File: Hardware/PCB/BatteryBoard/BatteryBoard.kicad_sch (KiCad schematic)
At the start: 79 parts, among them J1 USB_C_Receptacle_USB2.0, J2 Thermistor, J3 Conn_01x07, J4 Conn_01x07, J5 Conn_01x07, J6 Conn_01x07, J7 Power, Q1 FDS4935A, Q2 FDS4935A, SW1 SW_SPDT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

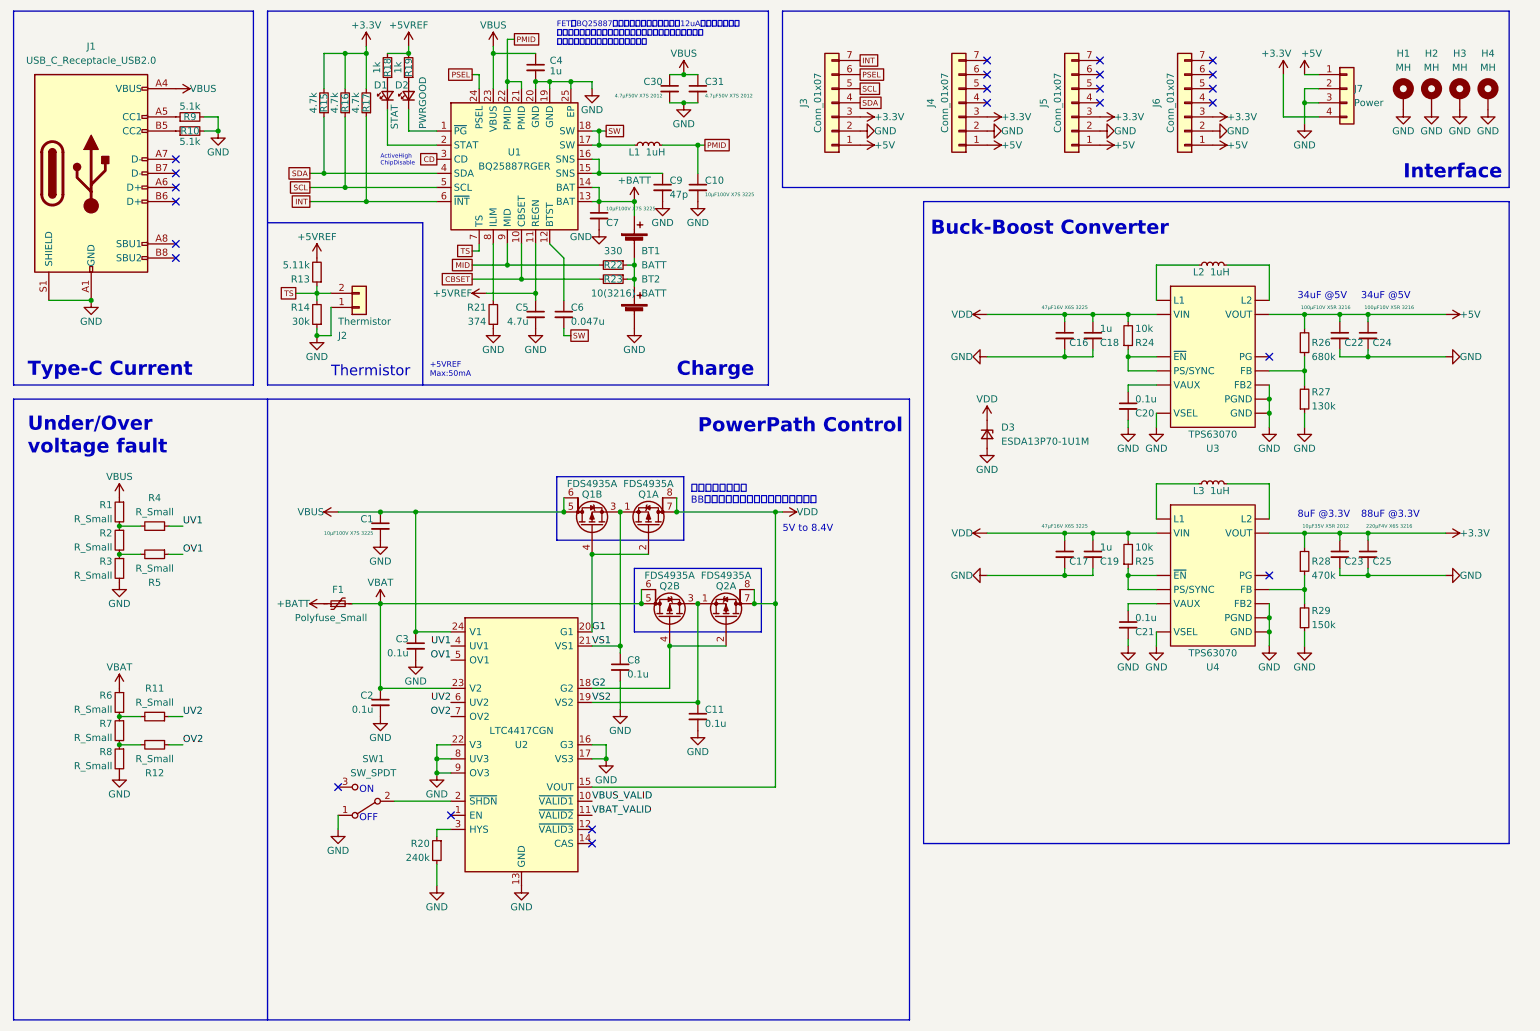
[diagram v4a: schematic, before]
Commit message: 電源ボード製作完了、抵抗の値を反映
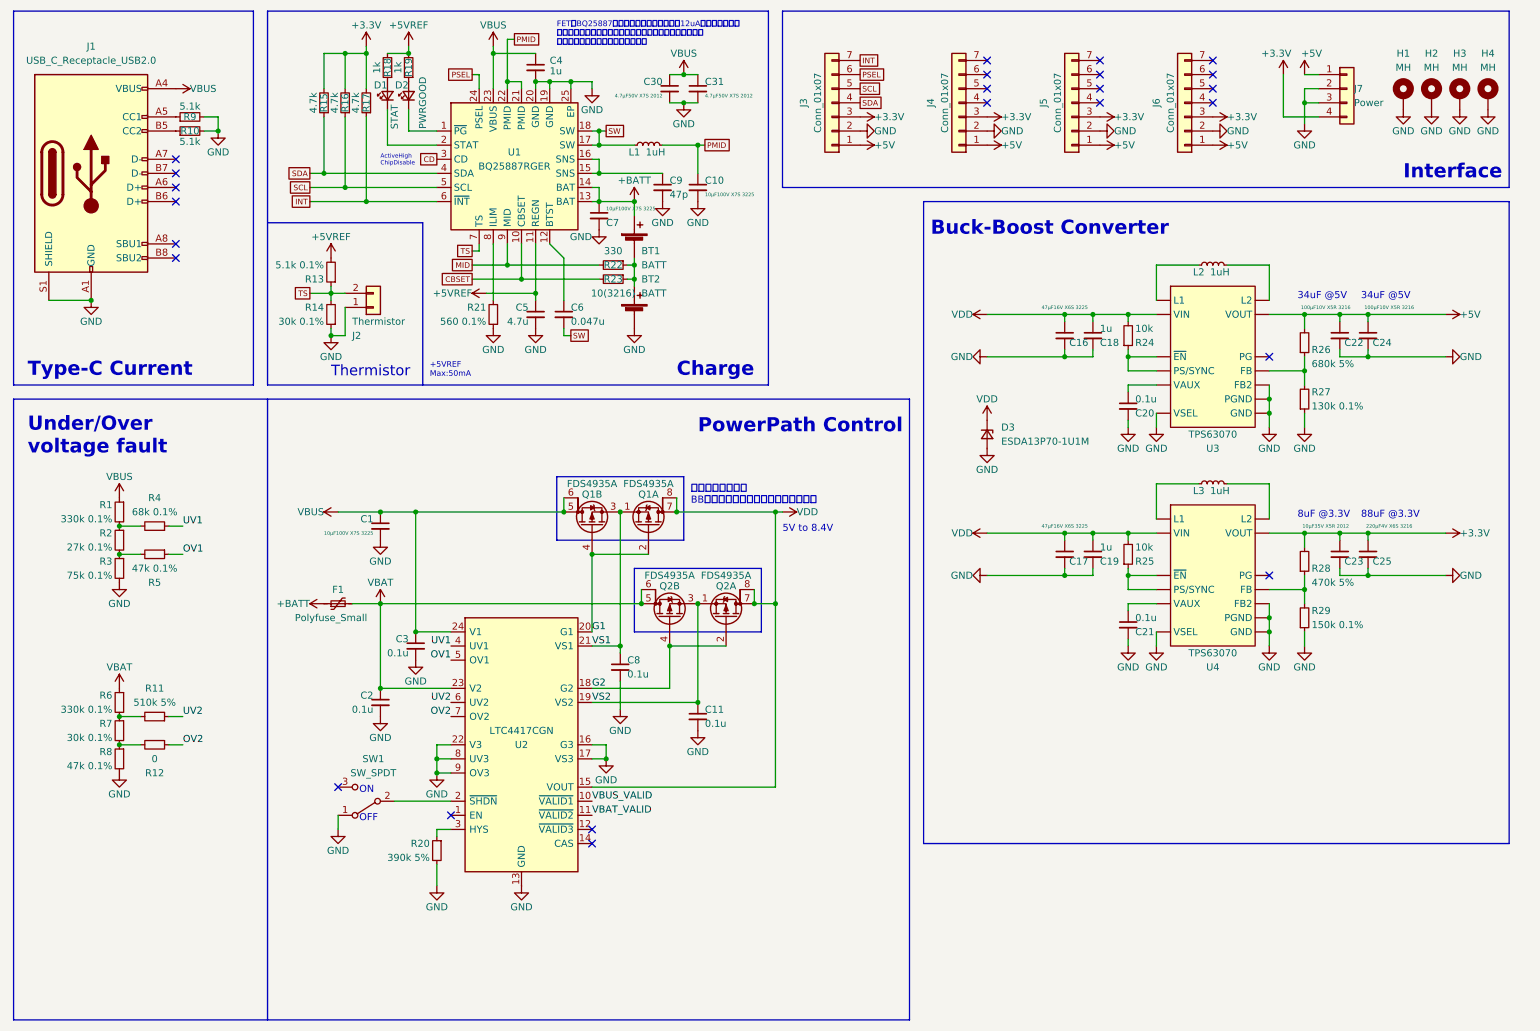
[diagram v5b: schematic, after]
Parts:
- R1, R6: value R_Small -> 330k 0.1%
- R11: value R_Small -> 510k 5%
- R12: value R_Small -> 0
- R13: value 5.11k -> 5.1k 0.1%
- R14: value 30k -> 30k 0.1%
- R2: value R_Small -> 27k 0.1%
- R20: value 240k -> 390k 5%
- R21: value 374 -> 560 0.1%
- R26: value 680k -> 680k 5%
- R27: value 130k -> 130k 0.1%
- R28: value 470k -> 470k 5%
- R29: value 150k -> 150k 0.1%
- R3: value R_Small -> 75k 0.1%
- R4: value R_Small -> 68k 0.1%
- R5, R8: value R_Small -> 47k 0.1%
- R7: value R_Small -> 30k 0.1%
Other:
- moved on the sheet: J2, R13, R14
